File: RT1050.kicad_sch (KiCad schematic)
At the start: 0 parts

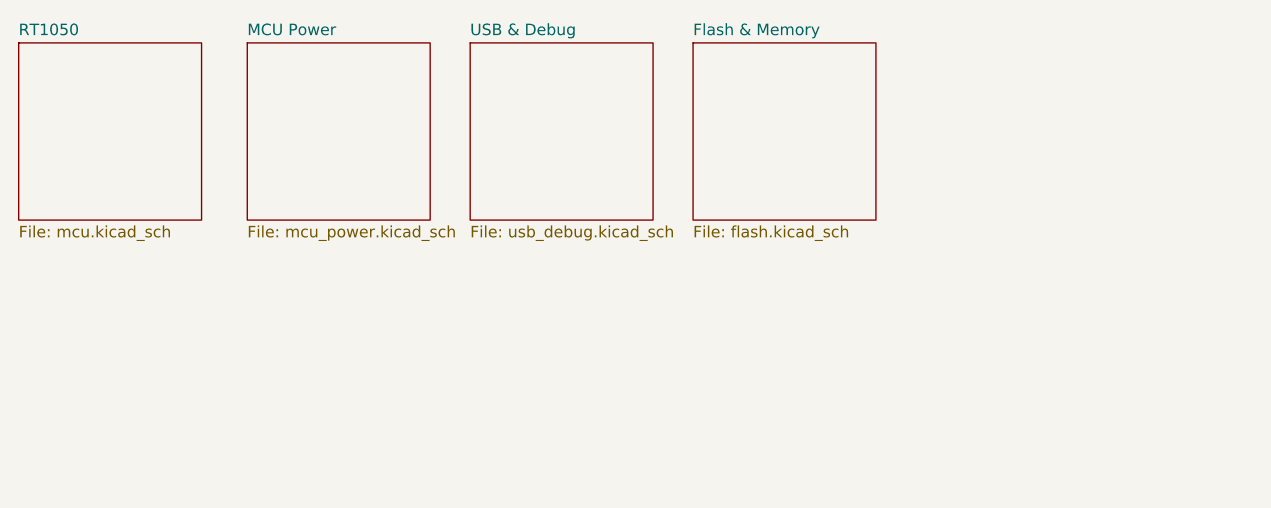
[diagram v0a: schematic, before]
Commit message: assign pin functions and started spe
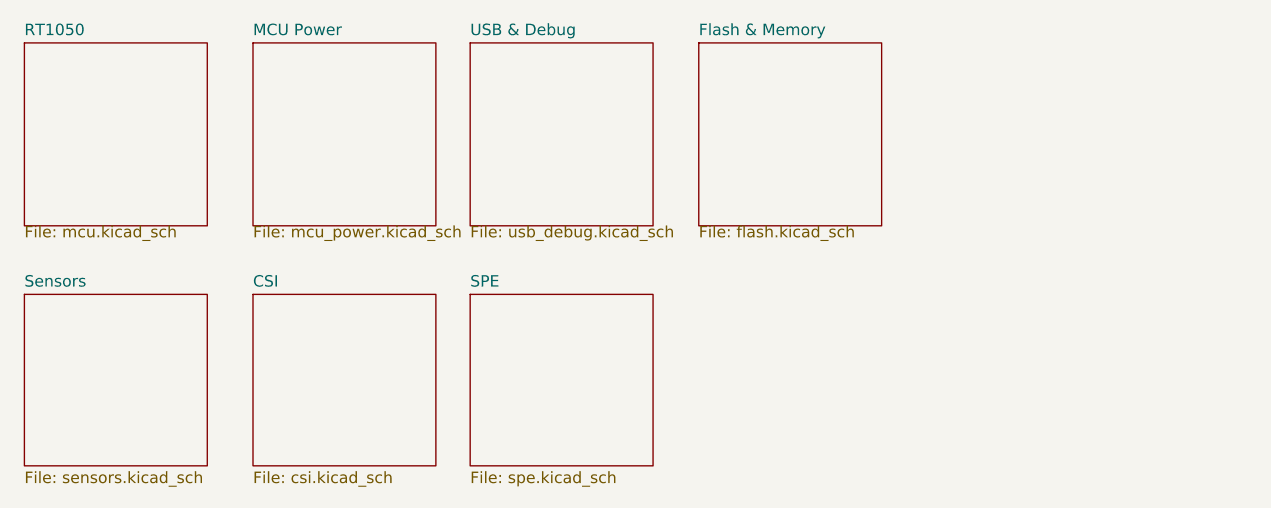
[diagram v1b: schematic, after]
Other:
- added sheet CSI (csi.kicad_sch)
- added sheet SPE (spe.kicad_sch)
- added sheet Sensors (sensors.kicad_sch)
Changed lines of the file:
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@@
 	(paper "A4")
 	(sheet
-		(at 88.265 15.24)
-		(size 20.32 19.685)
+		(at 13.97 43.18)
+		(size 20.32 19.05)
+		(fields_autoplaced yes)
+		(stroke
+			(width 0.1524)
+			(type solid)
+		)
+		(fill
+			(color 0 0 0 0.0000)
+		)
+		(property "Sheetname" "Sensors"
+			(at 13.97 42.4684 0)
+			(effects
+				(font
+					(size 1.27 1.27)
+				)
+				(justify left bottom)
+			)
+		)
+		(property "Sheetfile" "sensors.kicad_sch"
+			(at 13.97 62.8146 0)
+			(effects
+				(font
+					(size 1.27 1.27)
+				)
+				(justify left top)
+			)
+		)
+		(instances
+			(project "RT1050"
+				(path "/dd9d031d-43a1-4442-b493-27451a14e0d9"
+					(page "6")
+				)
+			)
+		)
+	)
+	(sheet
+		(at 88.9 15.24)
+		(size 20.32 20.32)
 		(fields_autoplaced yes)
 		(stroke
@@
 		)
 		(property "Sheetname" "Flash & Memory"
-			(at 88.265 14.5284 0)
+			(at 88.9 14.5284 0)
 			(effects
 				(font
@@
 		)
 		(property "Sheetfile" "flash.kicad_sch"
-			(at 88.265 35.5096 0)
+			(at 88.9 35.5096 0)
 			(effects
 				(font
@@
 	)
 	(sheet
+		(at 63.5 43.18)
+		(size 20.32 19.05)
+		(fields_autoplaced yes)
+		(stroke
+			(width 0.1524)
+			(type solid)
+		)
+		(fill
+			(color 0 0 0 0.0000)
+		)
+		(property "Sheetname" "SPE"
+			(at 63.5 42.4684 0)
+			(effects
+				(font
+					(size 1.27 1.27)
+				)
+				(justify left bottom)
+			)
+		)
+		(property "Sheetfile" "spe.kicad_sch"
+			(at 63.5 62.8146 0)
+			(effects
+				(font
+					(size 1.27 1.27)
+				)
+				(justify left top)
+			)
+		)
+		(instances
+			(project "RT1050"
+				(path "/dd9d031d-43a1-4442-b493-27451a14e0d9"
+					(page "8")
+				)
+			)
+		)
+	)
+	(sheet
+		(at 39.37 43.18)
+		(size 20.32 19.05)
+		(fields_autoplaced yes)
+		(stroke
+			(width 0.1524)
+			(type solid)
+		)
+		(fill
+			(color 0 0 0 0.0000)
+		)
+		(property "Sheetname" "CSI"
+			(at 39.37 42.4684 0)
+			(effects
+				(font
+					(size 1.27 1.27)
+				)
+				(justify left bottom)
+			)
+		)
+		(property "Sheetfile" "csi.kicad_sch"
+			(at 39.37 62.8146 0)
+			(effects
+				(font
+					(size 1.27 1.27)
+				)
+				(justify left top)
+			)
+		)
+		(instances
+			(project "RT1050"
+				(path "/dd9d031d-43a1-4442-b493-27451a14e0d9"
+					(page "7")
+				)
+			)
+		)
+	)
+	(sheet
 		(at 63.5 15.24)
-		(size 20.32 19.685)
+		(size 20.32 20.32)
 		(fields_autoplaced yes)
 		(stroke
@@
 	)
 	(sheet
-		(at 38.735 15.24)
-		(size 20.32 19.685)
+		(at 39.37 15.24)
+		(size 20.32 20.32)
 		(fields_autoplaced yes)
 		(stroke
@@
 		)
 		(property "Sheetname" "MCU Power"
-			(at 38.735 14.5284 0)
+			(at 39.37 14.5284 0)
 			(effects
 				(font
@@
 		)
 		(property "Sheetfile" "mcu_power.kicad_sch"
-			(at 38.735 35.5096 0)
+			(at 39.37 35.5096 0)
 			(effects
 				(font
@@
 	)
 	(sheet
-		(at 13.335 15.24)
-		(size 20.32 19.685)
+		(at 13.97 15.24)
+		(size 20.32 20.32)
 		(fields_autoplaced yes)
 		(stroke
@@
 		)
 		(property "Sheetname" "RT1050"
-			(at 13.335 14.5284 0)
+			(at 13.97 14.5284 0)
 			(effects
 				(font
@@
 		)
 		(property "Sheetfile" "mcu.kicad_sch"
-			(at 13.335 35.5096 0)
-			(effects
-				(font
+			(at 13.97 35.5096 0)
+			(effects
+				(font

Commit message: finished v1
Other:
- added sheet CAN Bus (can.kicad_sch)
- added sheet Connectors (connectors.kicad_sch)
- added sheet HopeRF (hoperf.kicad_sch)
- company: (none) -> Northeastern University
- title: (none) -> RT1050 DevBoard for Project Horizon
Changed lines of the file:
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@@
 	(generator "eeschema")
 	(generator_version "8.0")
-	(paper "A4")
+	(paper "A5")
+	(title_block
+		(title "RT1050 DevBoard for Project Horizon")
+		(rev "v1")
+		(company "Northeastern University")
+		(comment 1 "Built by Madhav Kapa")
+	)
+	(sheet
+		(at 119.38 15.24)
+		(size 20.32 20.32)
+		(fields_autoplaced yes)
+		(stroke
+			(width 0.1524)
+			(type solid)
+		)
+		(fill
+			(color 0 0 0 0.0000)
+		)
+		(property "Sheetname" "CAN Bus"
+			(at 119.38 14.5284 0)
+			(effects
+				(font
+					(size 1.27 1.27)
+				)
+				(justify left bottom)
+			)
+		)
+		(property "Sheetfile" "can.kicad_sch"
+			(at 119.38 36.1446 0)
+			(effects
+				(font
+					(size 1.27 1.27)
+				)
+				(justify left top)
+			)
+		)
+		(instances
+			(project "RT1050"
+				(path "/dd9d031d-43a1-4442-b493-27451a14e0d9"
+					(page "10")
+				)
+			)
+		)
+	)
 	(sheet
 		(at 13.97 43.18)
@@
 	)
 	(sheet
-		(at 88.9 15.24)
+		(at 93.98 15.24)
 		(size 20.32 20.32)
 		(fields_autoplaced yes)
@@
 		)
 		(property "Sheetname" "Flash & Memory"
-			(at 88.9 14.5284 0)
+			(at 93.98 14.5284 0)
 			(effects
 				(font
@@
 		)
 		(property "Sheetfile" "flash.kicad_sch"
-			(at 88.9 35.5096 0)
+			(at 93.98 35.5096 0)
 			(effects
 				(font
@@
 	)
 	(sheet
-		(at 63.5 43.18)
+		(at 119.38 43.18)
+		(size 20.32 19.05)
+		(fields_autoplaced yes)
+		(stroke
+			(width 0.1524)
+			(type solid)
+		)
+		(fill
+			(color 0 0 0 0.0000)
+		)
+		(property "Sheetname" "Connectors"
+			(at 119.38 42.4684 0)
+			(effects
+				(font
+					(size 1.27 1.27)
+				)
+				(justify left bottom)
+			)
+		)
+		(property "Sheetfile" "connectors.kicad_sch"
+			(at 119.38 62.8146 0)
+			(effects
+				(font
+					(size 1.27 1.27)
+				)
+				(justify left top)
+			)
+		)
+		(instances
+			(project "RT1050"
+				(path "/dd9d031d-43a1-4442-b493-27451a14e0d9"
+					(page "11")
+				)
+			)
+		)
+	)
+	(sheet
+		(at 67.31 43.18)
 		(size 20.32 19.05)
 		(fields_autoplaced yes)
@@
 		)
 		(property "Sheetname" "SPE"
-			(at 63.5 42.4684 0)
+			(at 67.31 42.4684 0)
 			(effects
 				(font
@@
 		)
 		(property "Sheetfile" "spe.kicad_sch"
-			(at 63.5 62.8146 0)
+			(at 67.31 62.8146 0)
 			(effects
 				(font
@@
 	)
 	(sheet
-		(at 39.37 43.18)
+		(at 40.64 43.18)
 		(size 20.32 19.05)
 		(fields_autoplaced yes)
@@
 		)
 		(property "Sheetname" "CSI"
-			(at 39.37 42.4684 0)
+			(at 40.64 42.4684 0)
 			(effects
 				(font
@@
 		)
 		(property "Sheetfile" "csi.kicad_sch"
-			(at 39.37 62.8146 0)
+			(at 40.64 62.8146 0)
 			(effects
 				(font
@@
 	)
 	(sheet
-		(at 63.5 15.24)
+		(at 67.31 15.24)
 		(size 20.32 20.32)
 		(fields_autoplaced yes)
@@
 		)
 		(property "Sheetname" "USB & Debug"
-			(at 63.5 14.5284 0)
+			(at 67.31 14.5284 0)
 			(effects
 				(font
@@
 		)
 		(property "Sheetfile" "usb_debug.kicad_sch"
-			(at 63.5 35.5096 0)
+			(at 67.31 35.5096 0)
 			(effects
 				(font
@@
 	)
 	(sheet
-		(at 39.37 15.24)
+		(at 40.64 15.24)
 		(size 20.32 20.32)
 		(fields_autoplaced yes)
@@
 		)
 		(property "Sheetname" "MCU Power"
-			(at 39.37 14.5284 0)
+			(at 40.64 14.5284 0)
 			(effects
 				(font
@@
 		)
 		(property "Sheetfile" "mcu_power.kicad_sch"
-			(at 39.37 35.5096 0)
+			(at 40.64 35.5096 0)
 			(effects
 				(font
@@
 				)
 			)
+		)
+	)
+	(sheet
+		(at 93.98 43.18)
+		(size 20.32 19.05)
+		(fields_autoplaced yes)
+		(stroke
+			(width 0.1524)
+			(type solid)
+		)
+		(fill
+			(color 0 0 0 0.0000)
+		)
+		(property "Sheetname" "HopeRF"
+			(at 93.98 42.4684 0)
+			(effects
+				(font
+					(size 1.27 1.27)
+				)
+				(justify left bottom)
+			)
+		)
+		(property "Sheetfile" "hoperf.kicad_sch"
+			(at 93.98 62.8146 0)
+			(effects
+				(font
+					(size 1.27 1.27)
+				)
+				(justify left top)
+			)
+		)
+		(instances
+			(project "RT1050"
+				(path "/dd9d031d-43a1-4442-b493-27451a14e0d9"
+					(page "11")
+				)
+			)
